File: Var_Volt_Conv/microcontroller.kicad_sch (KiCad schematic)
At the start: 14 parts

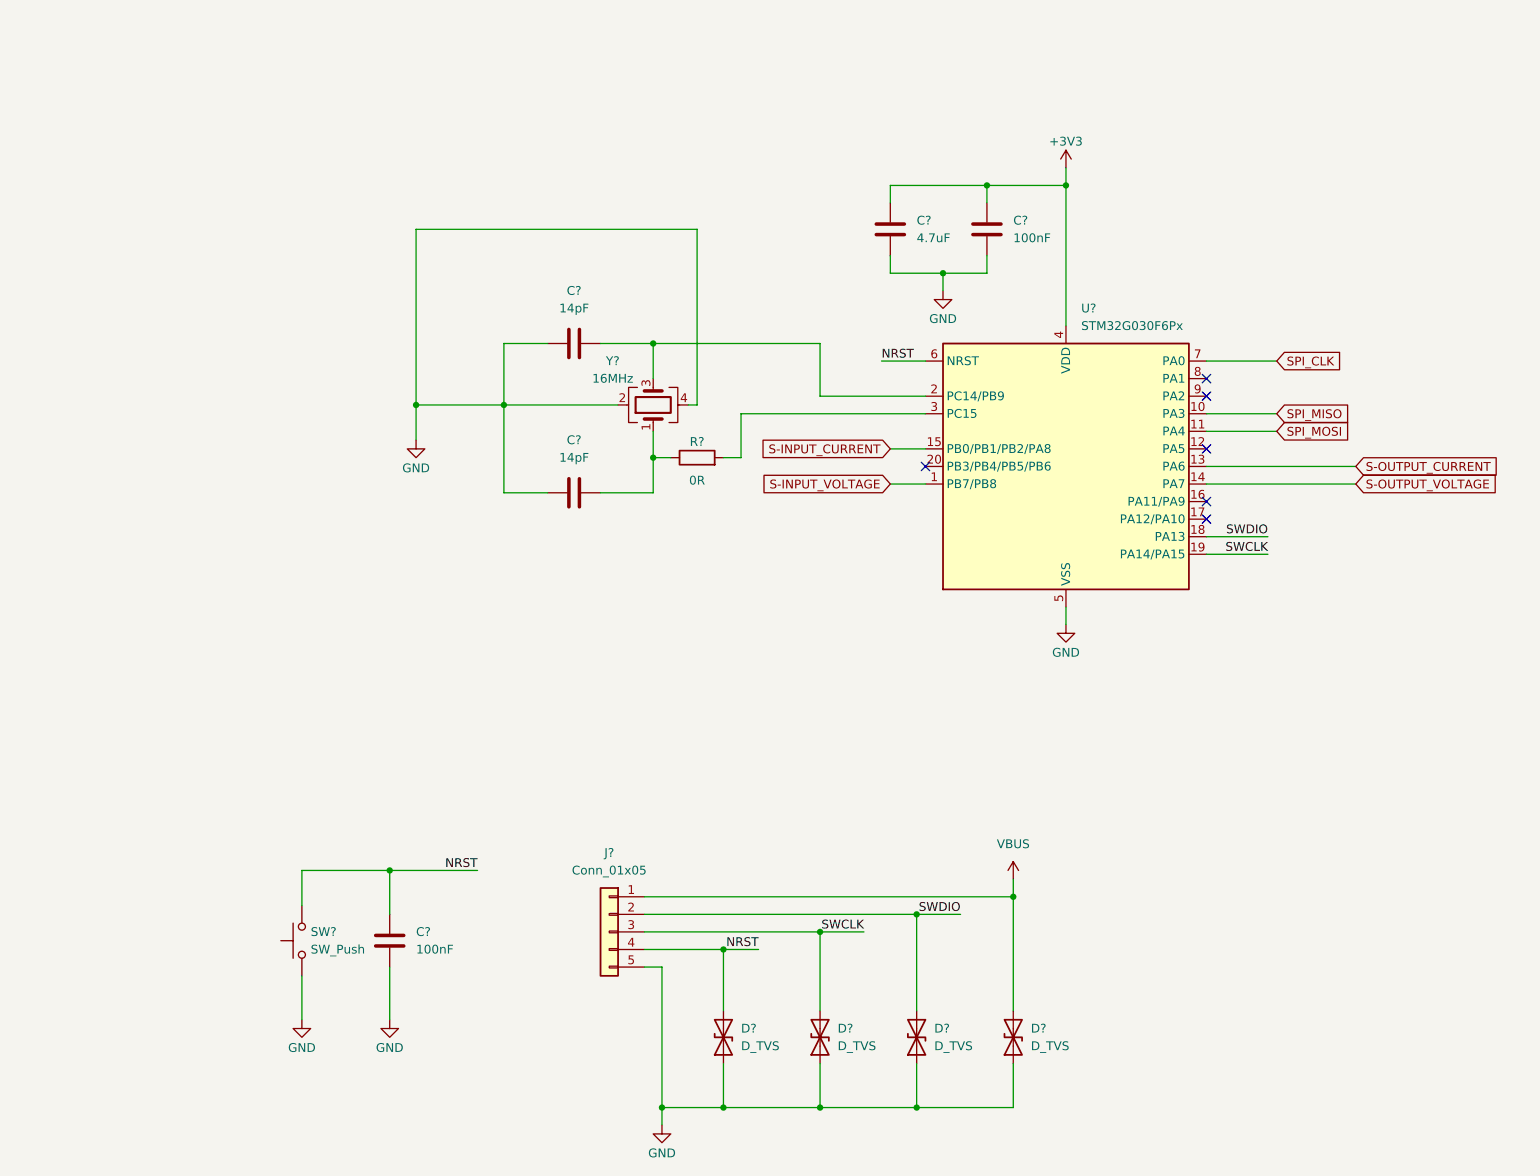
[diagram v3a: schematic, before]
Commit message: Tidied up microcontoller schematic
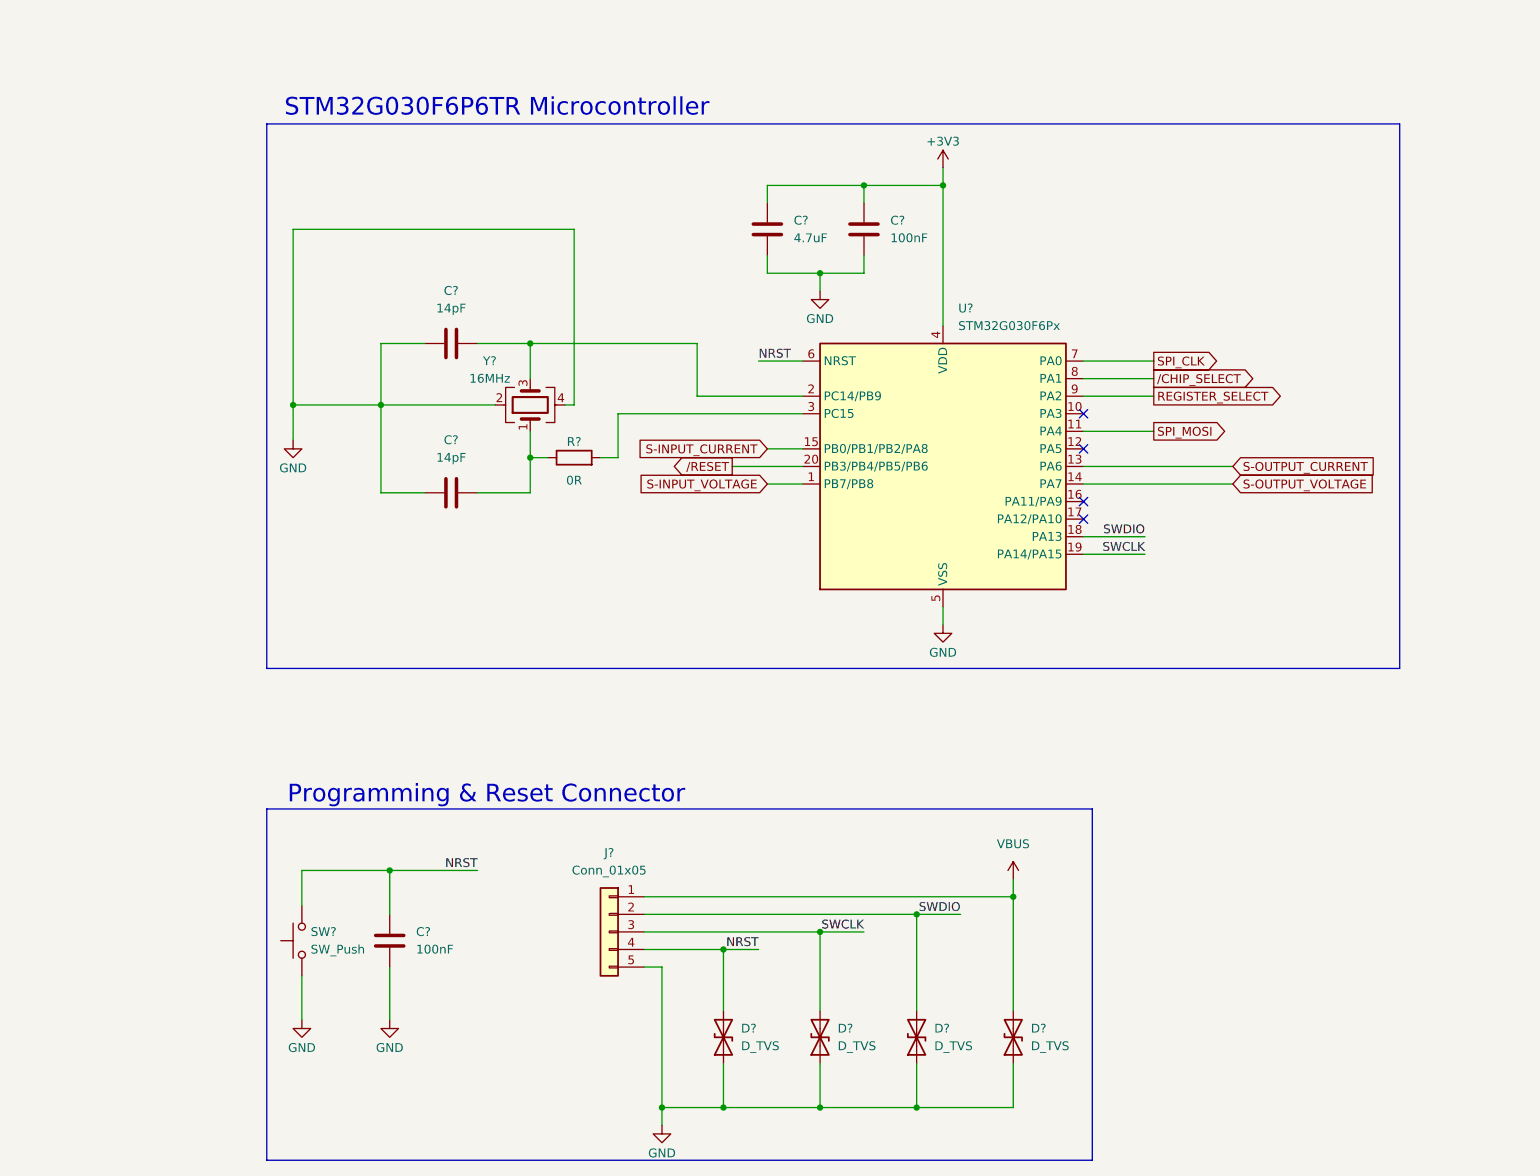
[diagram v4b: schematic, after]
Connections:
- net /RESET: now reaches U?.20 (PB3/PB4/PB5/PB6)
- net /CHIP_SELECT: now reaches U?.8 (PA1)
- net REGISTER_SELECT: now reaches U?.9 (PA2)
- net SPI_MISO: no longer names the net of U?.10 (PA3)
- no-connect marks 6 -> 4
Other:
- note added: "Programming & Reset Connector"
- note added: "STM32G030F6P6TR Microcontroller"
- moved on the sheet: C?, R?, U?, Y?

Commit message: Add bounding boxes and title/labels to all the sub-circuits
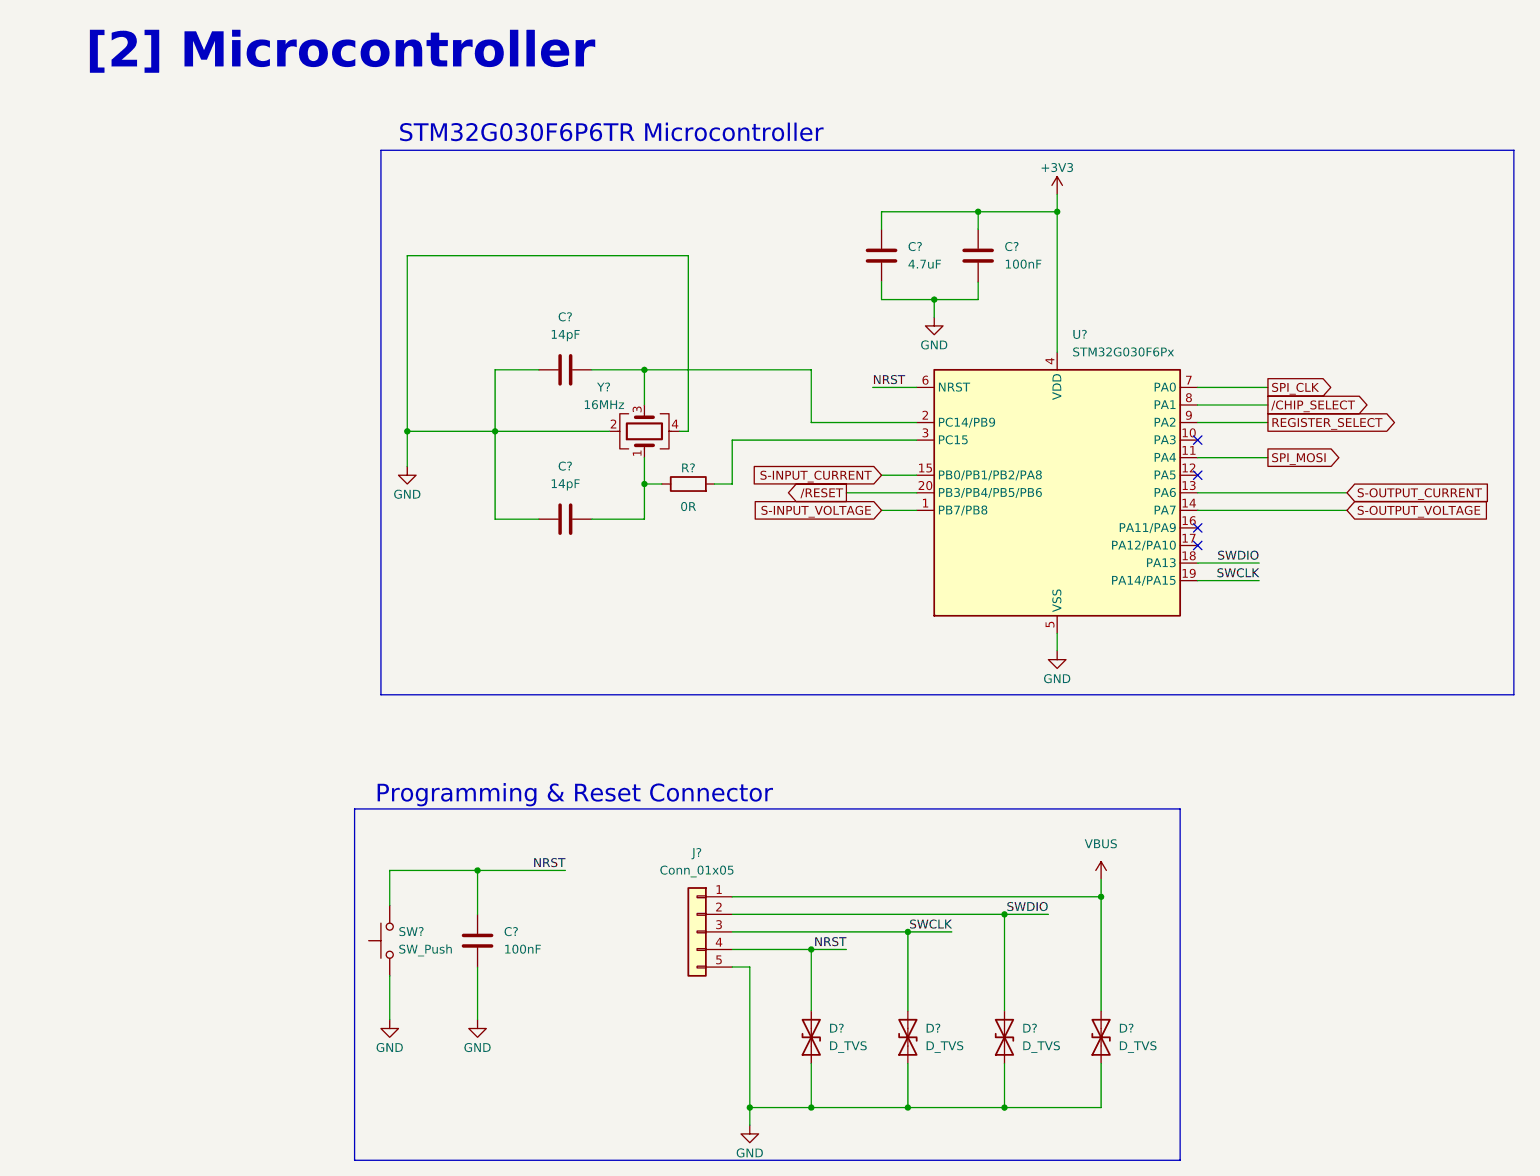
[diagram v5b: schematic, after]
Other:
- note added: "[2] Microcontroller"
- moved on the sheet: C?, D?, J?, R?, SW?, U?, Y?

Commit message: Rename power nets and integrated current sensing into power circuit
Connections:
- net VBUS renamed ST_3V3
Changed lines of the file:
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@@
 	(paper "A4")
+	(junction
+		(at 96.52 82.55)
+		(diameter 0)
+		(color 0 0 0 0)
+	)
 	(junction
 		(at 162.56 142.24)
@@
 	)
 	(junction
-		(at 96.52 82.55)
-		(diameter 0)
-		(color 0 0 0 0)
-	)
-	(junction
 		(at 138.43 55.88)
 		(diameter 0)
@@
 	(wire
 		(pts
-			(xy 162.56 139.7) (xy 162.56 142.24)
-		)
-		(stroke
-			(width 0)
-			(type default)
-		)
-	)
-	(wire
-		(pts
 			(xy 96.52 78.74) (xy 96.52 82.55)
 		)
@@
 	(wire
 		(pts
+			(xy 162.56 134.62) (xy 162.56 142.24)
+		)
+		(stroke
+			(width 0)
+			(type default)
+		)
+	)
+	(wire
+		(pts
 			(xy 176.53 68.58) (xy 186.69 68.58)
 		)
@@
 		(pts
 			(xy 135.89 76.2) (xy 109.22 76.2)
+		)
+		(stroke
+			(width 0)
+			(type default)
+		)
+	)
+	(wire
+		(pts
+			(xy 163.83 134.62) (xy 162.56 134.62)
 		)
 		(stroke
@@
 		(property "Intersheetrefs" "${INTERSHEET_REFS}"
 			(at 220.639 83.82 0)
+			(effects
+				(font
+					(size 1.27 1.27)
+				)
+				(justify left)
+				(hide yes)
+			)
+		)
+	)
+	(global_label "ST_3V3"
+		(shape input)
+		(at 163.83 134.62 0)
+		(fields_autoplaced yes)
+		(effects
+			(font
+				(size 1.27 1.27)
+			)
+			(justify left)
+		)
+		(property "Intersheetrefs" "${INTERSHEET_REFS}"
+			(at 173.4675 134.62 0)
 			(effects
 				(font
@@
 					(unit 1)
 				)
-			)
-		)
-	)
-	(symbol
-		(lib_id "power:VBUS")
-		(at 162.56 139.7 0)
-		(unit 1)
-		(exclude_from_sim no)
-		(in_bom yes)
-		(on_board yes)
-		(dnp no)
-		(fields_autoplaced yes)
-		(property "Reference" "#PWR08"
-			(at 162.56 143.51 0)
-			(effects
-				(font
-					(size 1.27 1.27)
-				)
-				(hide yes)
-			)
-		)
-		(property "Value" "VBUS"
-			(at 162.56 134.62 0)
-			(effects
-				(font
-					(size 1.27 1.27)
-				)
-			)
-		)
-		(property "Footprint" ""
-			(at 162.56 139.7 0)
-			(effects
-				(font
-					(size 1.27 1.27)
-				)
-				(hide yes)
-			)
-		)
-		(property "Datasheet" ""
-			(at 162.56 139.7 0)
-			(effects
-				(font
-					(size 1.27 1.27)
-				)
-				(hide yes)
-			)
-		)
-		(property "Description" "Power symbol creates a global label with name \"VBUS\""
-			(at 162.56 139.7 0)
-			(effects
-				(font
-					(size 1.27 1.27)
-				)
-				(hide yes)
-			)
-		)
-		(pin "1"
-		)
-		(instances
-			(project ""
-				(path "/7c9580d6-c22f-4506-b9c3-9272e882c9fb/b048280b-6fef-4656-96bb-ca0a0c35ac5b"
-					(reference "#PWR08")
-					(unit 1)
-				)

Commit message: Added microcontroller notes, and power indicator LED
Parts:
- C? (x2): value 100nF -> 0.1uF
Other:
- note added: "Crystal: 7U16000E12UCG Load Capacitance: 12 pF Assumed Stray Capacitance: 5pF Cl = 2*(12pF-5pF) ESR = 60 ohm (max)"
- note added: "TVS/ESD Diodes: PESD3V3L1BA"
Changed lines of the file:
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@@
+		)
+	)
+	(text "TVS/ESD Diodes: PESD3V3L1BA"
+		(exclude_from_sim no)
+		(at 140.97 176.022 0)
+		(effects
+			(font
+				(size 1.27 1.27)
+			)
 		)
 	)
@@
 				(size 2.54 2.54)
 			)
+		)
+	)
+	(text "Crystal: 7U16000E12UCG\nLoad Capacitance: 12 pF\nAssumed Stray Capacitance: 5pF\nCl = 2*(12pF-5pF)\nESR = 60 ohm (max)"
+		(exclude_from_sim no)
+		(at 82.55 98.044 0)
+		(effects
+			(font
+				(size 1.27 1.27)
+			)
+			(justify left)
 		)
 	)
@@
 			)
 		)
-		(property "Value" "100nF"
+		(property "Value" "0.1uF"
 			(at 148.59 50.7999 0)
 			(effects
@@
 			)
 		)
-		(property "Value" "100nF"
+		(property "Value" "0.1uF"
 			(at 76.2 149.8599 0)
 			(effects

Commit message: Annotated schematic symbols
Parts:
- gave numbers to parts that had none: 14
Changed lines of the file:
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@@
 		(dnp no)
 		(fields_autoplaced yes)
-		(property "Reference" "SW?"
+		(property "Reference" "SW201"
 			(at 60.96 147.3199 90)
 			(effects
@@
 			(project ""
 				(path "/7c9580d6-c22f-4506-b9c3-9272e882c9fb/b048280b-6fef-4656-96bb-ca0a0c35ac5b"
-					(reference "SW?")
+					(reference "SW201")
 					(unit 1)
 				)
@@
 		(dnp no)
 		(fields_autoplaced yes)
-		(property "Reference" "C?"
+		(property "Reference" "C201"
 			(at 134.62 48.2599 0)
 			(effects
@@
 			(project "Var_Volt_Conv"
 				(path "/7c9580d6-c22f-4506-b9c3-9272e882c9fb/b048280b-6fef-4656-96bb-ca0a0c35ac5b"
-					(reference "C?")
+					(reference "C201")
 					(unit 1)
 				)
@@
 		(dnp no)
 		(fields_autoplaced yes)
-		(property "Reference" "D?"
+		(property "Reference" "D204"
 			(at 165.1 161.2899 90)
 			(effects
@@
 			(project "Var_Volt_Conv"
 				(path "/7c9580d6-c22f-4506-b9c3-9272e882c9fb/b048280b-6fef-4656-96bb-ca0a0c35ac5b"
-					(reference "D?")
+					(reference "D204")
 					(unit 1)
 				)
@@
 		(dnp no)
 		(fields_autoplaced yes)
-		(property "Reference" "C?"
+		(property "Reference" "C203"
 			(at 85.09 58.42 90)
 			(effects
@@
 			(project ""
 				(path "/7c9580d6-c22f-4506-b9c3-9272e882c9fb/b048280b-6fef-4656-96bb-ca0a0c35ac5b"
-					(reference "C?")
+					(reference "C203")
 					(unit 1)
 				)
@@
 		(on_board yes)
 		(dnp no)
-		(property "Reference" "Y?"
+		(property "Reference" "Y201"
 			(at 90.678 68.58 90)
 			(effects
@@
 			(project ""
 				(path "/7c9580d6-c22f-4506-b9c3-9272e882c9fb/b048280b-6fef-4656-96bb-ca0a0c35ac5b"
-					(reference "Y?")
+					(reference "Y201")
 					(unit 1)
 				)
@@
 		(dnp no)
 		(fields_autoplaced yes)
-		(property "Reference" "D?"
+		(property "Reference" "D202"
 			(at 137.16 161.2899 90)
 			(effects
@@
 			(project "Var_Volt_Conv"
 				(path "/7c9580d6-c22f-4506-b9c3-9272e882c9fb/b048280b-6fef-4656-96bb-ca0a0c35ac5b"
-					(reference "D?")
+					(reference "D202")
 					(unit 1)
 				)
@@
 		(dnp no)
 		(fields_autoplaced yes)
-		(property "Reference" "C?"
+		(property "Reference" "C204"
 			(at 85.09 80.01 90)
 			(effects
@@
 			(project "Var_Volt_Conv"
 				(path "/7c9580d6-c22f-4506-b9c3-9272e882c9fb/b048280b-6fef-4656-96bb-ca0a0c35ac5b"
-					(reference "C?")
+					(reference "C204")
 					(unit 1)
 				)
@@
 		(dnp no)
 		(fields_autoplaced yes)
-		(property "Reference" "J?"
+		(property "Reference" "J201"
 			(at 104.14 135.89 0)
 			(effects
@@
 			(project ""
 				(path "/7c9580d6-c22f-4506-b9c3-9272e882c9fb/b048280b-6fef-4656-96bb-ca0a0c35ac5b"
-					(reference "J?")
+					(reference "J201")
 					(unit 1)
 				)
@@
 		(dnp no)
 		(fields_autoplaced yes)
-		(property "Reference" "D?"
+		(property "Reference" "D203"
 			(at 151.13 161.2899 90)
 			(effects
@@
 			(project "Var_Volt_Conv"
 				(path "/7c9580d6-c22f-4506-b9c3-9272e882c9fb/b048280b-6fef-4656-96bb-ca0a0c35ac5b"
-					(reference "D?")
+					(reference "D203")
 					(unit 1)
 				)
@@
 		(on_board yes)
 		(dnp no)
-		(property "Reference" "R?"
+		(property "Reference" "R201"
 			(at 102.87 80.264 90)
 			(effects
@@
 			(project ""
 				(path "/7c9580d6-c22f-4506-b9c3-9272e882c9fb/b048280b-6fef-4656-96bb-ca0a0c35ac5b"
-					(reference "R?")
+					(reference "R201")
 					(unit 1)
 				)
@@
 		(dnp no)
 		(fields_autoplaced yes)
-		(property "Reference" "D?"
+		(property "Reference" "D201"
 			(at 123.19 161.2899 90)
 			(effects
@@
 			(project ""
 				(path "/7c9580d6-c22f-4506-b9c3-9272e882c9fb/b048280b-6fef-4656-96bb-ca0a0c35ac5b"
-					(reference "D?")
+					(reference "D201")
 					(unit 1)
 				)
@@
 		(dnp no)
 		(fields_autoplaced yes)
-		(property "Reference" "C?"
+		(property "Reference" "C202"
 			(at 148.59 48.2599 0)
 			(effects
@@
 			(project ""
 				(path "/7c9580d6-c22f-4506-b9c3-9272e882c9fb/b048280b-6fef-4656-96bb-ca0a0c35ac5b"
-					(reference "C?")
+					(reference "C202")
 					(unit 1)
 				)
@@
 		(dnp no)
 		(fields_autoplaced yes)
-		(property "Reference" "U?"
+		(property "Reference" "U201"
 			(at 158.4041 60.96 0)
 			(effects
@@
 			(project ""
 				(path "/7c9580d6-c22f-4506-b9c3-9272e882c9fb/b048280b-6fef-4656-96bb-ca0a0c35ac5b"
-					(reference "U?")
+					(reference "U201")
 					(unit 1)
 				)
@@
 		(dnp no)
 		(fields_autoplaced yes)
-		(property "Reference" "C?"
+		(property "Reference" "C205"
 			(at 76.2 147.3199 0)
 			(effects
@@
 			(project "Var_Volt_Conv"
 				(path "/7c9580d6-c22f-4506-b9c3-9272e882c9fb/b048280b-6fef-4656-96bb-ca0a0c35ac5b"
-					(reference "C?")
-					(unit 1)
-				)
+					(reference "C205")
+					(unit 1)
+				)
